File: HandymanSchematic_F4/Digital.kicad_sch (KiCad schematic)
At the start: 38 parts, among them J1 SWD Header, J2 Jacks, Q2 2N7002, Q3 2N7002, SW1 RST, SW2 BYP, U1 SH1106, U3 STM32F411RETx, U4 AMS1117, Y1 16MHz

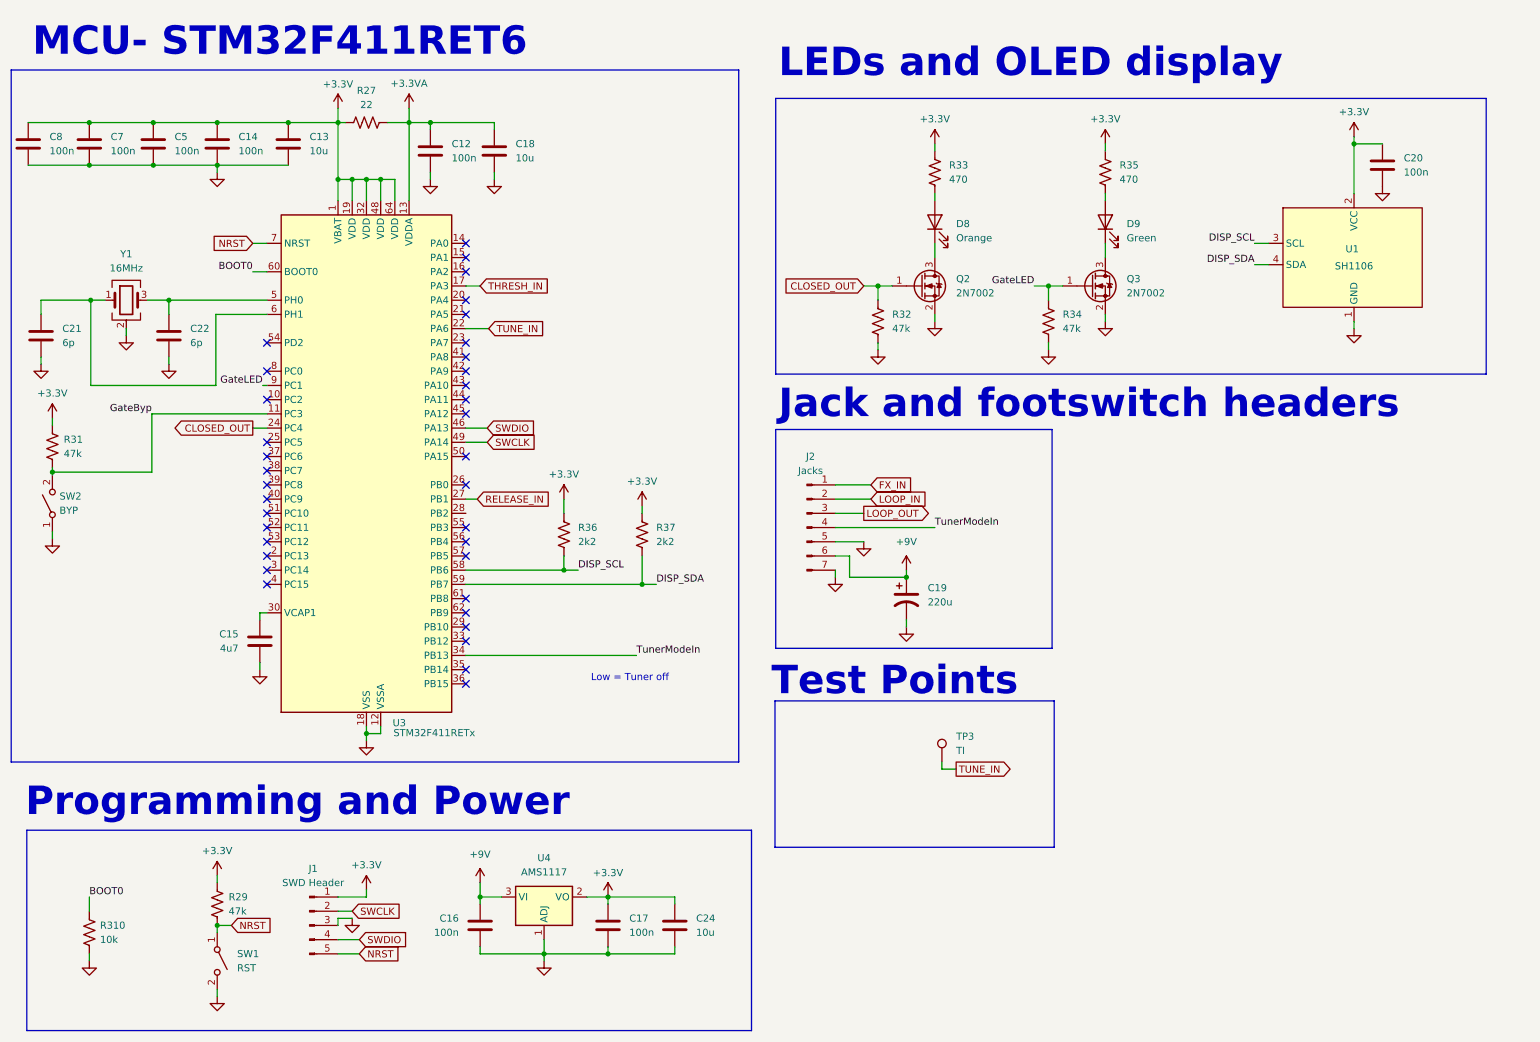
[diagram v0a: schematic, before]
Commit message: schematic changes for DFM
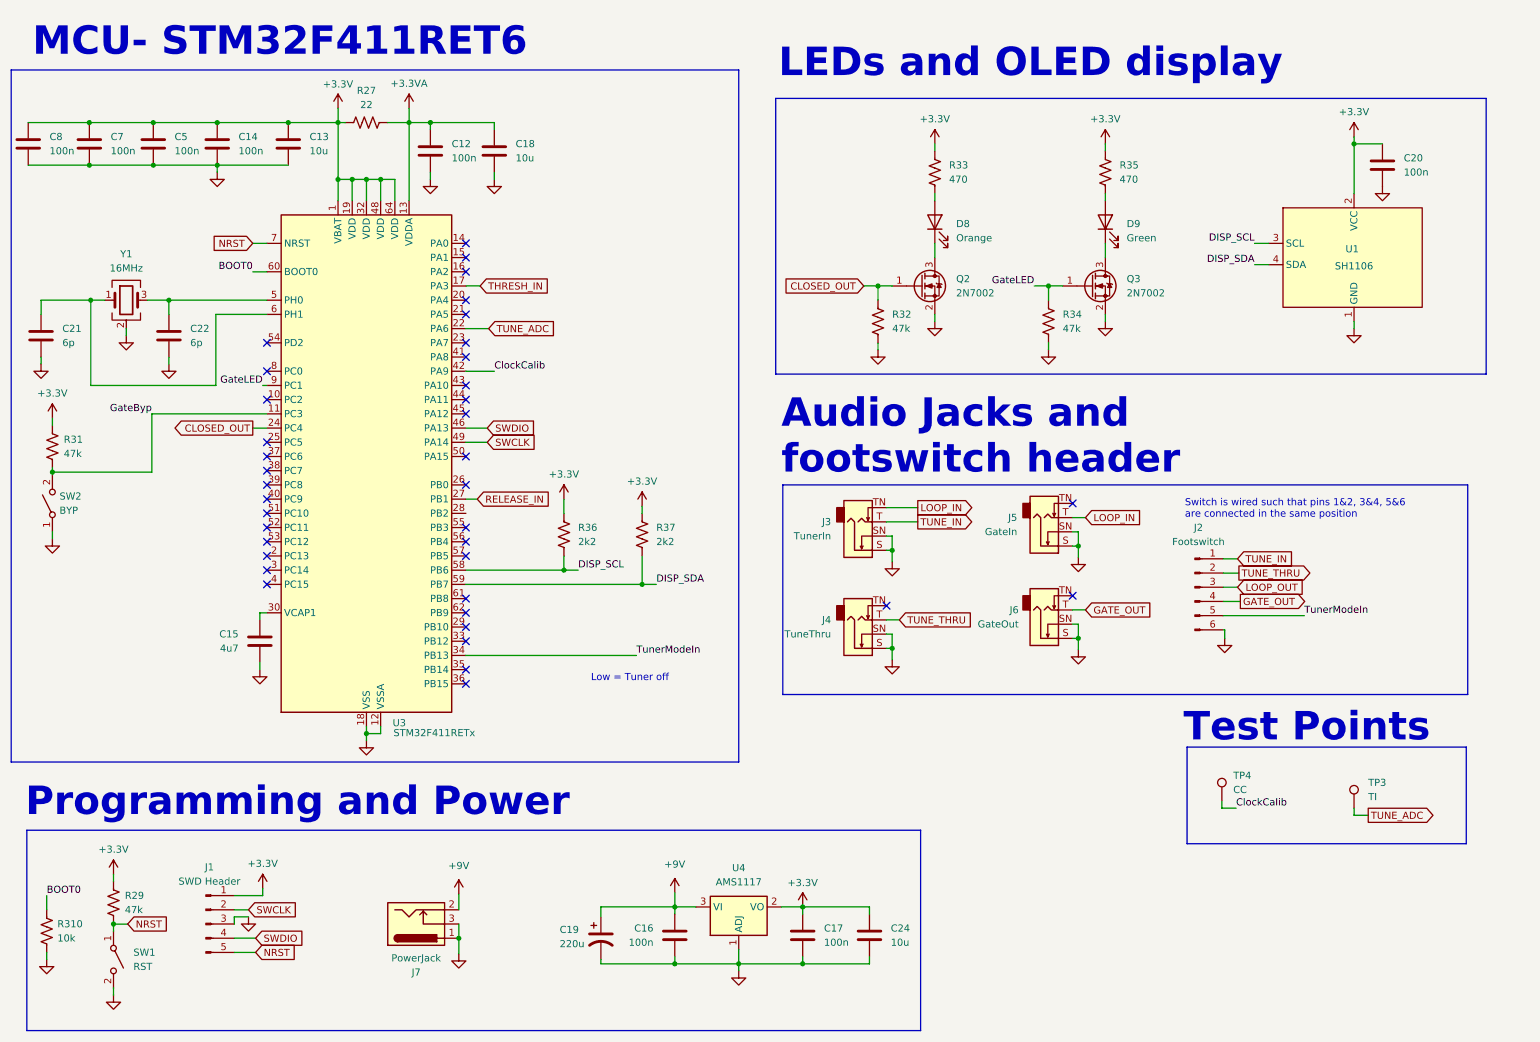
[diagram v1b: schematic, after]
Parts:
- removed J2: Jacks, Connector_PinSocket_2.54mm:PinSocket_1x07_P2.54mm_Vertical, symbol Connector:Conn_01x07_Pin
- added J2: Footswitch, symbol Connector:Conn_01x06_Pin
- added J3: TunerIn, symbol Connector_Audio:AudioJack2_Switch
- added J4: TuneThru, symbol Connector_Audio:AudioJack2_Switch
- added J5: GateIn, symbol Connector_Audio:AudioJack2_Switch
- added J6: GateOut, symbol Connector_Audio:AudioJack2_Switch
- added J7: PowerJack, Connector_BarrelJack:BarrelJack_Horizontal, symbol Connector:Barrel_Jack_Switch
- added TP4: CC, TestPoint:TestPoint_THTPad_D2.0mm_Drill1.0mm_VAL, symbol Connector:TestPoint
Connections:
- net +9V: now also J7.2
- net GND: now also J2.6 (Pin_6), J3.S, J3.SN, J4.S, J4.SN, J5.S, J5.SN, J6.S, J6.SN, J7.1, J7.3
- net LOOP_IN: now also J3.TN, J5.T
- net LOOP_OUT: now also J2.3 (Pin_3)
- net TUNE_IN: now also J2.1 (Pin_1), J3.T; no longer TP3.1, U3.22 (PA6)
- net TunerModeIn: now also J2.5 (Pin_5)
- net ClockCalib: now reaches U3.42 (PA9)
- net ClockCalib: now also TP4.1
- new net GATE_OUT: J2.4 (Pin_4), J6.T
- new net TUNE_ADC: TP3.1, U3.22 (PA6)
- new net TUNE_THRU: J2.2 (Pin_2), J4.T
- no-connect marks 36 -> 38
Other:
- note added: "Audio Jacks and footswitch header"
- note added: "Switch is wired such that pins 1&2, 3&4, 5&6 are connected in the same position"
- note removed: "Jack and footswitch headers"
- moved on the sheet: C16, C17, C19, C24, J1, R29, R310, SW1, TP3, U4

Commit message: routed, DRC passing
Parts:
- J2: footprint (none) -> Connector_PinHeader_2.54mm:PinHeader_1x06_P2.54mm_Vertical
- J3, J4, J5, J6: footprint (none) -> Connector_Audio:Jack_6.35mm_Tayda_PJ664C_Mono_Horizontal
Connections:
- no-connect marks 38 -> 39
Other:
- moved on the sheet: J3, J4, J5, J6, TP3, TP4

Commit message: set up BOM w supplier links fixing merge conflict
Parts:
- C12, C14, C16, C17, C20, C5, C7, C8: MPN (none) -> KGF21BR71H104KT; Purchase Link (none) -> https://www.mouser.com/en/ProductDetail/KYOCERA-AVX/KGF21BR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
- C13, C18, C24: MPN (none) -> KGM21AR50J106KU; Purchase Link (none) -> https://www.mouser.com/en/ProductDetail/KYOCERA-AVX/KGM21AR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
- C15: MPN (none) -> CGA4J3X7R1A475K125AB; Purchase Link (none) -> https://www.mouser.com/en/ProductDetail/TDK/CGA4J3X7R1A475K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
- C19: value 220u -> 100u; MPN (none) -> ESH107M010AC3AA; Purchase Link (none) -> https://www.mouser.com/en/ProductDetail/KEMET/ESH107M010AC3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
- C21, C22: MPN (none) -> 0805N6R0D500CT; Purchase Link (none) -> https://www.mouser.com/en/ProductDetail/Walsin/0805N6R0D500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
- D8: MPN (none) -> LTL-4291N; Purchase Link (none) -> https://www.mouser.com/en/ProductDetail/LITEON/LTL-4291N?qs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
- D9: MPN (none) -> LTL-4231N; Purchase Link (none) -> https://www.mouser.com/en/ProductDetail/LITEON/LTL-4231N?qs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
- J1, SW1: now not fitted
- J2: MPN (none) -> SF17N-0302-21R-L-1.1KG-R; Purchase Link (none) -> https://www.taydaelectronics.com/electromechanical/switches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
- J3, J4, J5, J6: MPN (none) -> PJ-644C MONO; Purchase Link (none) -> https://www.taydaelectronics.com/6-35mm-1-4-stereo-insulate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
- J7: MPN (none) -> NEB 21 R-C; Purchase Link (none) -> https://www.taydaelectronics.com/hardware-tools/dc-power/ne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
- Q2, Q3: MPN (none) -> 2N7002NXAKR; Purchase Link (none) -> https://www.mouser.com/en/ProductDetail/Nexperia/2N7002NXAK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
- R27: MPN (none) -> RC0805JR-0722RL; Purchase Link (none) -> https://www.mouser.com/en/ProductDetail/YAGEO/RC0805JR-0722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
- R29, R31, R32, R34: MPN (none) -> RK73B2ATTE473J; Purchase Link (none) -> https://www.mouser.com/en/ProductDetail/KOA-Speer/RK73B2ATT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
- R310: MPN (none) -> AC0805JR-0710KL; Purchase Link (none) -> https://www.mouser.com/en/ProductDetail/YAGEO/AC0805JR-0710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
- R33, R35: MPN (none) -> RC0805JR-10470RL; Purchase Link (none) -> https://www.mouser.com/en/ProductDetail/YAGEO/RC0805JR-1047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
- R36, R37: MPN (none) -> AC0805FR-072K2L; Purchase Link (none) -> https://www.mouser.com/en/ProductDetail/YAGEO/AC0805FR-072K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
- SW2: MPN (none) -> TS02-66-90-BK-100-SCR-D; Purchase Link (none) -> https://www.mouser.com/en/ProductDetail/Same-Sky/TS02-66-90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
- U1: MPN (none) -> SH1106; Purchase Link (none) -> https://www.amazon.com/dp/B0C3L7N917?ref=ppx_yo2ov_dt_b_fed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
- U3: MPN (none) -> STM32F411RET6TR; Purchase Link (none) -> https://www.mouser.com/en/ProductDetail/STMicroelectronics/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
- U4: MPN (none) -> LD1117S33CTR; Purchase Link (none) -> https://www.mouser.com/en/ProductDetail/511-LD1117S33C
- Y1: MPN (none) -> CX3225FB16000B0FZZH1; Purchase Link (none) -> https://www.mouser.com/en/ProductDetail/KYOCERA-AVX/CX3225F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

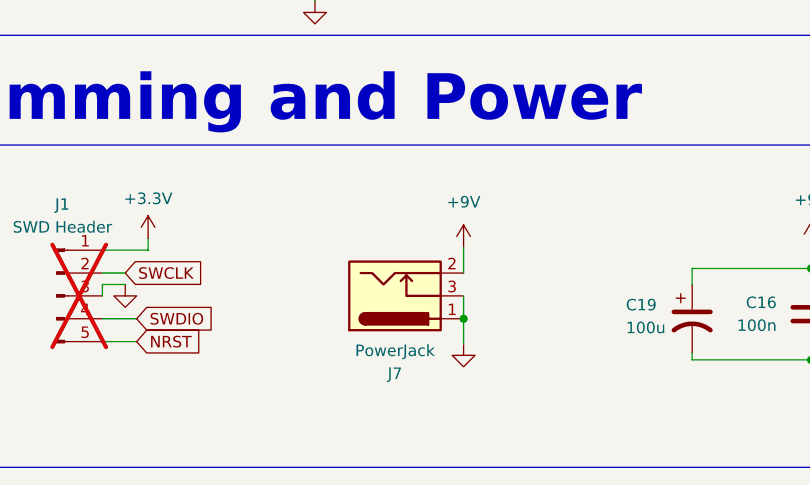
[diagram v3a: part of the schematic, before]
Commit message: added ground spring, rev5 at fab
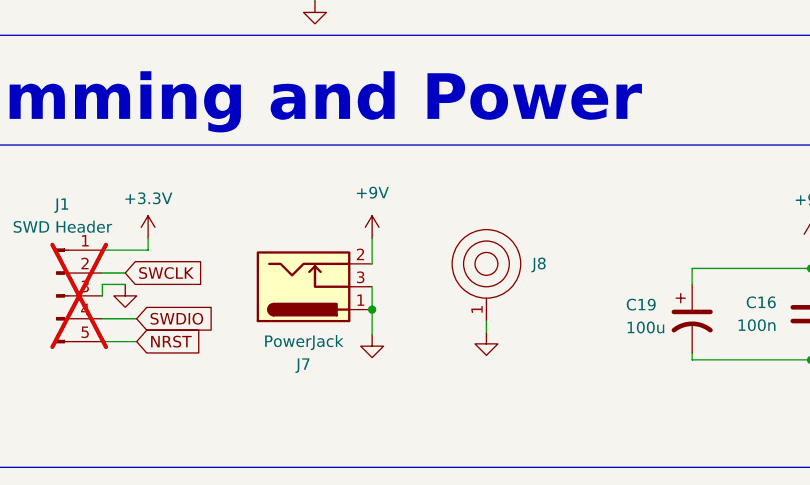
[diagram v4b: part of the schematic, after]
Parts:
- added J8: (no value), Connector:BatteryContact_Keystone_243, symbol Connector:GroundingSpring
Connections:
- net GND: now also J8.1
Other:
- moved on the sheet: J7
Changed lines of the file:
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@@
 	)
 	(junction
-		(at 92.71 177.546)
+		(at 82.55 176.53)
 		(diameter 0)
 		(color 0 0 0 0)
@@
 	(wire
 		(pts
-			(xy 92.71 175.006) (xy 92.71 177.546)
+			(xy 82.55 173.99) (xy 82.55 176.53)
 		)
 		(stroke
@@
 	(wire
 		(pts
-			(xy 92.71 169.672) (xy 92.71 172.466)
+			(xy 82.55 168.656) (xy 82.55 171.45)
 		)
 		(stroke
@@
 	(wire
 		(pts
+			(xy 95.25 177.8) (xy 95.25 179.07)
+		)
+		(stroke
+			(width 0)
+			(type default)
+		)
+	)
+	(wire
+		(pts
 			(xy 118.11 182.118) (xy 131.318 182.118)
 		)
@@
 	(wire
 		(pts
-			(xy 92.71 177.546) (xy 92.71 180.34)
+			(xy 82.55 176.53) (xy 82.55 179.324)
 		)
 		(stroke
@@
 	(symbol
 		(lib_id "power:GND")
-		(at 92.71 180.34 0)
+		(at 82.55 179.324 0)
 		(unit 1)
 		(body_style 1)
@@
 		(fields_autoplaced yes)
 		(property "Reference" "#PWR036"
-			(at 92.71 186.69 0)
+			(at 82.55 185.674 0)
 			(hide yes)
 			(show_name no)
@@
 		)
 		(property "Value" "GND"
-			(at 92.71 185.42 0)
+			(at 82.55 184.404 0)
 			(hide yes)
 			(show_name no)
@@
 		)
 		(property "Footprint" ""
-			(at 92.71 180.34 0)
+			(at 82.55 179.324 0)
 			(hide yes)
 			(show_name no)
@@
 		)
 		(property "Datasheet" ""
-			(at 92.71 180.34 0)
+			(at 82.55 179.324 0)
 			(hide yes)
 			(show_name no)
@@
 		)
 		(property "Description" ""
-			(at 92.71 180.34 0)
+			(at 82.55 179.324 0)
 			(hide yes)
 			(show_name no)
@@
 	(symbol
 		(lib_id "PCM_4ms_Power-symbol:+9V")
-		(at 92.71 169.672 0)
+		(at 82.55 168.656 0)
 		(unit 1)
 		(body_style 1)
@@
 		(fields_autoplaced yes)
 		(property "Reference" "#PWR030"
-			(at 92.71 173.482 0)
+			(at 82.55 172.466 0)
 			(hide yes)
 			(show_name no)
@@
 		)
 		(property "Value" "+9V"
-			(at 92.71 164.592 0)
+			(at 82.55 163.576 0)
 			(show_name no)
 			(do_not_autoplace no)
@@
 		)
 		(property "Footprint" ""
-			(at 92.71 169.672 0)
+			(at 82.55 168.656 0)
 			(hide yes)
 			(show_name no)
@@
 		)
 		(property "Datasheet" ""
-			(at 92.71 169.672 0)
+			(at 82.55 168.656 0)
 			(hide yes)
 			(show_name no)
@@
 		)
 		(property "Description" "Power symbol creates a global label with name \"+9V\""
-			(at 92.71 169.672 0)
+			(at 82.55 168.656 0)
 			(hide yes)
 			(show_name no)
@@
 	)
 	(symbol
+		(lib_id "power:GND")
+		(at 95.25 179.07 0)
+		(unit 1)
+		(body_style 1)
+		(exclude_from_sim no)
+		(in_bom yes)
+		(on_board yes)
+		(in_pos_files yes)
+		(dnp no)
+		(fields_autoplaced yes)
+		(property "Reference" "#PWR037"
+			(at 95.25 185.42 0)
+			(hide yes)
+			(show_name no)
+			(do_not_autoplace no)
+			(effects
+				(font
+					(size 1.27 1.27)
+				)
+			)
+		)
+		(property "Value" "GND"
+			(at 95.25 184.15 0)
+			(hide yes)
+			(show_name no)
+			(do_not_autoplace no)
+			(effects
+				(font
+					(size 1.27 1.27)
+				)
+			)
+		)
+		(property "Footprint" ""
+			(at 95.25 179.07 0)
+			(hide yes)
+			(show_name no)
+			(do_not_autoplace no)
+			(effects
+				(font
+					(size 1.27 1.27)
+				)
+			)
+		)
+		(property "Datasheet" ""
+			(at 95.25 179.07 0)
+			(hide yes)
+			(show_name no)
+			(do_not_autoplace no)
+			(effects
+				(font
+					(size 1.27 1.27)
+				)
+			)
+		)
+		(property "Description" ""
+			(at 95.25 179.07 0)
+			(hide yes)
+			(show_name no)
+			(do_not_autoplace no)
+			(effects
+				(font
+					(size 1.27 1.27)
+				)
+			)
+		)
+		(pin "1"
+		)
+		(instances
+			(project "HandymanSchematic_F4"
+				(path "/bc3da82e-d0a7-49a6-b9ec-ecd2040670ff/887caaef-7a77-44c5-aff2-1e54e61c47e4"
+					(reference "#PWR037")
+					(unit 1)
+				)
+			)
+		)
+	)
+	(symbol
 		(lib_id "Device:R_US")
 		(at 19.05 176.276 0)
@@
 	)
 	(symbol
+		(lib_id "Connector:GroundingSpring")
+		(at 95.25 175.26 0)
+		(unit 1)
+		(body_style 1)
+		(exclude_from_sim no)
+		(in_bom yes)
+		(on_board yes)
+		(in_pos_files yes)
+		(dnp no)
+		(fields_autoplaced yes)
+		(property "Reference" "J8"
+			(at 100.33 171.4499 0)
+			(show_name no)
+			(do_not_autoplace no)
+			(effects
+				(font
+					(size 1.27 1.27)
+				)
+				(justify left)
+			)
+		)
+		(property "Value" ""
+			(at 95.25 175.26 0)
+			(show_name no)
+			(do_not_autoplace no)
+			(effects
+				(font
+					(size 1.27 1.27)
+				)
+			)
+		)
+		(property "Footprint" "Connector:BatteryContact_Keystone_243"
+			(at 95.25 175.26 0)
+			(hide yes)
+			(show_name no)
+			(do_not_autoplace no)
+			(effects
+				(font
+					(size 1.27 1.27)
+				)
+			)
+		)
+		(property "Datasheet" ""
+			(at 95.25 175.26 0)
+			(hide yes)
+			(show_name no)
+			(do_not_autoplace no)
+			(effects
+				(font
+					(size 1.27 1.27)
+				)
+			)
+		)
+		(property "Description" ""
+			(at 95.25 175.26 0)
+			(hide yes)
+			(show_name no)
+			(do_not_autoplace no)
+			(effects
+				(font
+					(size 1.27 1.27)
+				)
+			)
+		)
+		(pin "1"
+		)
+		(instances
+			(project "HandymanSchematic_F4"
+				(path "/bc3da82e-d0a7-49a6-b9ec-ecd2040670ff/887caaef-7a77-44c5-aff2-1e54e61c47e4"
+					(reference "J8")
+					(unit 1)
+				)
+			)
+		)
+	)
+	(symbol
 		(lib_id "Connector:Barrel_Jack_Switch")
-		(at 85.09 175.006 0)
+		(at 74.93 173.99 0)
 		(mirror x)
 		(unit 1)
@@
 		(dnp no)
 		(property "Reference" "J7"
-			(at 85.09 183.642 0)
+			(at 74.93 182.626 0)
 			(show_name no)
 			(do_not_autoplace no)
@@
 		)
 		(property "Value" "PowerJack"
-			(at 85.09 181.102 0)
+			(at 74.93 180.086 0)
 			(show_name no)
 			(do_not_autoplace no)
@@
 		)
 		(property "Footprint" "Connector_BarrelJack:BarrelJack_Horizontal"
-			(at 86.36 173.99 0)
+			(at 76.2 172.974 0)
 			(hide yes)
 			(show_name no)
@@
 		)
 		(property "Datasheet" ""
-			(at 86.36 173.99 0)
+			(at 76.2 172.974 0)
 			(hide yes)
 			(show_name no)
@@
 		)
 		(property "Description" "DC Barrel Jack with an internal switch"
-			(at 85.09 175.006 0)
+			(at 74.93 173.99 0)
 			(hide yes)
 			(show_name no)
@@
 		)
 		(property "MPN" "NEB 21 R-C"
-			(at 85.09 175.006 0)
+			(at 74.93 173.99 0)
 			(hide yes)
 			(show_name no)
@@
 		)
 		(property "Purchase Link" "https://www.taydaelectronics.com/hardware-tools/dc-power/neb-21-r-c-lumberg-dc-power-socket.html"
-			(at 85.09 175.006 0)
+			(at 74.93 173.99 0)
 			(hide yes)
 			(show_name no)
@@
 		)
 		(property "KLC_S3.3" ""
-			(at 85.09 175.006 0)
+			(at 74.93 173.99 0)
 			(hide yes)
 			(show_name no)
@@
 		)
 		(property "KLC_S4.1" ""
-			(at 85.09 175.006 0)
+			(at 74.93 173.99 0)
 			(hide yes)
 			(show_name no)
